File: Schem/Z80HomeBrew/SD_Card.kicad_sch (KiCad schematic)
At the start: 4 parts, among them J2 Micro_SD_Card_Det1, U17 4050

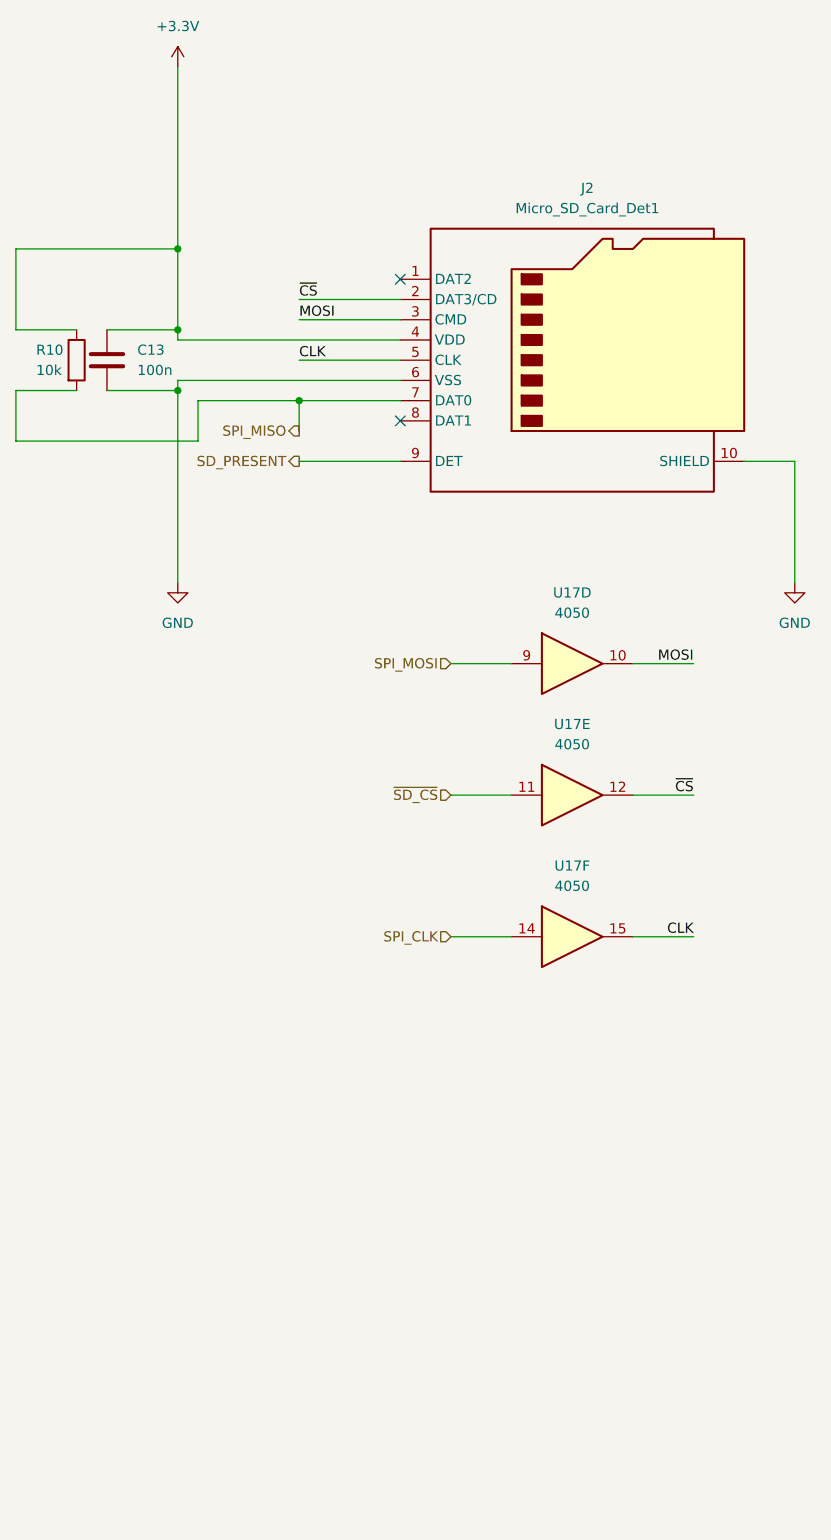
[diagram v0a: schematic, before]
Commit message: Video block added. fixed some issues with parts...
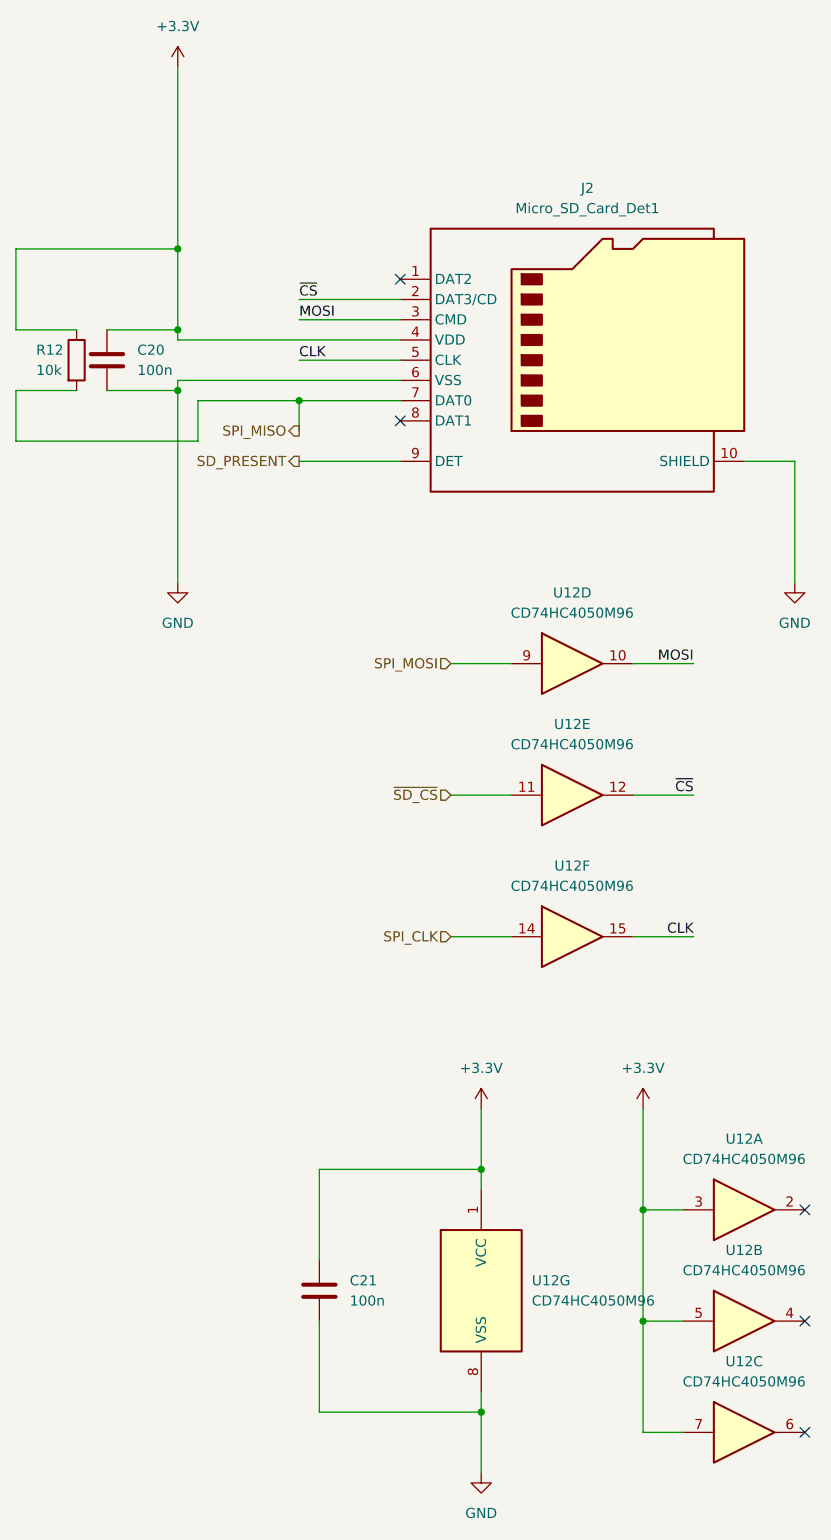
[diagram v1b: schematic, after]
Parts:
- added C21: 100n, Capacitor_SMD:C_0603_1608Metric, symbol Device:C
- added unit 3 of U12
- added unit 1 of U12
- added unit 7 of U12
- added unit 2 of U12
- U12: renamed from U17; value 4050 -> CD74HC4050M96; footprint (none) -> Footprints:SOIC127P600X175-16N
- renumbered C13 to C20, R10 to R12
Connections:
- net +3.3V: now also C21.1, U12.1 (VCC), U12.3, U12.5, U12.7
- net GND: now also C21.2, U12.8 (VSS)
- no-connect marks 2 -> 5

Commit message: Completed schematics
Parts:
- J2: value Micro_SD_Card_Det1 -> MSD-1-A; footprint (none) -> Footprints:CUI_MSD-1-A
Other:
- moved on the sheet: C21, R12, U12G
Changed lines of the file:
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@@
 	)
 	(junction
-		(at 88.9 195.58)
+		(at 83.82 195.58)
 		(diameter 0)
 		(color 0 0 0 0)
@@
 	)
 	(junction
-		(at 88.9 165.1)
+		(at 83.82 165.1)
 		(diameter 0)
 		(color 0 0 0 0)
@@
 	(wire
 		(pts
-			(xy 30.48 67.31) (xy 38.1 67.31)
-		)
-		(stroke
-			(width 0)
-			(type default)
-		)
-	)
-	(wire
-		(pts
 			(xy 128.27 76.2) (xy 128.27 91.44)
 		)
@@
 	(wire
 		(pts
-			(xy 88.9 165.1) (xy 88.9 167.64)
+			(xy 83.82 165.1) (xy 83.82 167.64)
 		)
 		(stroke
@@
 	(wire
 		(pts
-			(xy 88.9 157.48) (xy 88.9 165.1)
+			(xy 83.82 157.48) (xy 83.82 165.1)
 		)
 		(stroke
@@
 	(wire
 		(pts
-			(xy 30.48 67.31) (xy 30.48 73.66)
-		)
-		(stroke
-			(width 0)
-			(type default)
-		)
-	)
-	(wire
-		(pts
-			(xy 88.9 193.04) (xy 88.9 195.58)
+			(xy 36.83 67.31) (xy 36.83 73.66)
+		)
+		(stroke
+			(width 0)
+			(type default)
+		)
+	)
+	(wire
+		(pts
+			(xy 83.82 193.04) (xy 83.82 195.58)
 		)
 		(stroke
@@
 	(wire
 		(pts
-			(xy 68.58 165.1) (xy 88.9 165.1)
+			(xy 63.5 165.1) (xy 83.82 165.1)
 		)
 		(stroke
@@
 	(wire
 		(pts
-			(xy 30.48 49.53) (xy 50.8 49.53)
+			(xy 36.83 49.53) (xy 50.8 49.53)
 		)
 		(stroke
@@
 	(wire
 		(pts
-			(xy 30.48 59.69) (xy 38.1 59.69)
-		)
-		(stroke
-			(width 0)
-			(type default)
-		)
-	)
-	(wire
-		(pts
 			(xy 66.04 76.2) (xy 78.74 76.2)
 		)
@@
 	(wire
 		(pts
-			(xy 68.58 195.58) (xy 88.9 195.58)
+			(xy 63.5 195.58) (xy 83.82 195.58)
 		)
 		(stroke
@@
 	(wire
 		(pts
-			(xy 30.48 73.66) (xy 53.34 73.66)
-		)
-		(stroke
-			(width 0)
-			(type default)
-		)
-	)
-	(wire
-		(pts
-			(xy 68.58 184.15) (xy 68.58 195.58)
+			(xy 36.83 73.66) (xy 53.34 73.66)
+		)
+		(stroke
+			(width 0)
+			(type default)
+		)
+	)
+	(wire
+		(pts
+			(xy 63.5 184.15) (xy 63.5 195.58)
 		)
 		(stroke
@@
 	(wire
 		(pts
-			(xy 30.48 59.69) (xy 30.48 49.53)
-		)
-		(stroke
-			(width 0)
-			(type default)
-		)
-	)
-	(wire
-		(pts
-			(xy 68.58 176.53) (xy 68.58 165.1)
+			(xy 36.83 59.69) (xy 36.83 49.53)
+		)
+		(stroke
+			(width 0)
+			(type default)
+		)
+	)
+	(wire
+		(pts
+			(xy 63.5 176.53) (xy 63.5 165.1)
 		)
 		(stroke
@@
 	(wire
 		(pts
-			(xy 88.9 195.58) (xy 88.9 203.2)
+			(xy 83.82 195.58) (xy 83.82 203.2)
 		)
 		(stroke
@@
 			)
 		)
-		(property "Value" "Micro_SD_Card_Det1"
+		(property "Value" "MSD-1-A"
 			(at 102.235 44.45 0)
 			(effects
@@
 			)
 		)
-		(property "Footprint" ""
+		(property "Footprint" "Footprints:CUI_MSD-1-A"
 			(at 153.67 45.72 0)
 			(effects
@@
 			)
 		)
-		(property "Datasheet" "https://datasheet.lcsc.com/lcsc/2110151630_XKB-Connectivity-XKTF-015-N_C381082.pdf"
+		(property "Datasheet" "https://www.sameskydevices.com/product/resource/msd-4-a.pdf"
 			(at 101.6 60.96 0)
 			(effects
@@
 	(symbol
 		(lib_id "Device:C")
-		(at 68.58 180.34 0)
+		(at 63.5 180.34 0)
 		(unit 1)
 		(exclude_from_sim no)
@@
 		(fields_autoplaced yes)
 		(property "Reference" "C21"
-			(at 72.39 179.0699 0)
+			(at 67.31 179.0699 0)
 			(effects
 				(font
@@
 		)
 		(property "Value" "100n"
-			(at 72.39 181.6099 0)
+			(at 67.31 181.6099 0)
 			(effects
 				(font
@@
 		)
 		(property "Footprint" "Capacitor_SMD:C_0603_1608Metric"
-			(at 69.5452 184.15 0)
+			(at 64.4652 184.15 0)
 			(effects
 				(font
@@
 		)
 		(property "Datasheet" "~"
-			(at 68.58 180.34 0)
+			(at 63.5 180.34 0)
 			(effects
 				(font
@@
 		)
 		(property "Description" "Unpolarized capacitor"
-			(at 68.58 180.34 0)
+			(at 63.5 180.34 0)
 			(effects
 				(font
@@
 	(symbol
 		(lib_id "power:+3.3V")
-		(at 88.9 157.48 0)
+		(at 83.82 157.48 0)
 		(unit 1)
 		(exclude_from_sim no)
@@
 		(fields_autoplaced yes)
 		(property "Reference" "#PWR051"
-			(at 88.9 161.29 0)
+			(at 83.82 161.29 0)
 			(effects
 				(font
@@
 		)
 		(property "Value" "+3.3V"
-			(at 88.9 152.4 0)
+			(at 83.82 152.4 0)
 			(effects
 				(font
@@
 		)
 		(property "Footprint" ""
-			(at 88.9 157.48 0)
+			(at 83.82 157.48 0)
 			(effects
 				(font
@@
 		)
 		(property "Datasheet" ""
-			(at 88.9 157.48 0)
+			(at 83.82 157.48 0)
 			(effects
 				(font
@@
 		)
 		(property "Description" "Power symbol creates a global label with name \"+3.3V\""
-			(at 88.9 157.48 0)
+			(at 83.82 157.48 0)
 			(effects
 				(font
@@
 	(symbol
 		(lib_id "Device:R")
-		(at 38.1 63.5 0)
+		(at 36.83 63.5 0)
 		(unit 1)
 		(exclude_from_sim no)
@@
 		(dnp no)
 		(property "Reference" "R12"
-			(at 33.02 62.2299 0)
+			(at 31.75 62.2299 0)
 			(effects
 				(font
@@
 		)
 		(property "Value" "10k"
-			(at 33.02 64.7699 0)
+			(at 31.75 64.7699 0)
 			(effects
 				(font
@@
 		)
 		(property "Footprint" "Resistor_SMD:R_0603_1608Metric"
-			(at 36.322 63.5 90)
+			(at 35.052 63.5 90)
 			(effects
 				(font
@@
 		)
 		(property "Datasheet" "~"
-			(at 38.1 63.5 0)
+			(at 36.83 63.5 0)
 			(effects
 				(font
@@
 		)
 		(property "Description" "Resistor"
-			(at 38.1 63.5 0)
+			(at 36.83 63.5 0)
 			(effects
 				(font
@@
 	(symbol
 		(lib_id "4xxx:4050")
-		(at 88.9 180.34 0)
+		(at 83.82 180.34 0)
 		(unit 7)
 		(exclude_from_sim no)
@@
 		(fields_autoplaced yes)
 		(property "Reference" "U12"
-			(at 95.25 179.0699 0)
+			(at 90.17 179.0699 0)
 			(effects
 				(font
@@
 		)
 		(property "Value" "CD74HC4050M96"
-			(at 95.25 181.6099 0)
+			(at 90.17 181.6099 0)
 			(effects
 				(font
@@
 		)
 		(property "Footprint" "Footprints:SOIC127P600X175-16N"
-			(at 88.9 180.34 0)
+			(at 83.82 180.34 0)
 			(effects
 				(font
@@
 		)
 		(property "Datasheet" "http://www.intersil.com/content/dam/intersil/documents/cd40/cd4050bms.pdf"
-			(at 88.9 180.34 0)
+			(at 83.82 180.34 0)
 			(effects
 				(font
@@
 		)
 		(property "Description" "Hex Buffer"
-			(at 88.9 180.34 0)
+			(at 83.82 180.34 0)
 			(effects
 				(font
@@
 	(symbol
 		(lib_id "power:GND")
-		(at 88.9 203.2 0)
+		(at 83.82 203.2 0)
 		(unit 1)
 		(exclude_from_sim no)
@@
 		(fields_autoplaced yes)
 		(property "Reference" "#PWR053"
-			(at 88.9 209.55 0)
+			(at 83.82 209.55 0)
 			(effects
 				(font
@@
 		)
 		(property "Value" "GND"
-			(at 88.9 208.28 0)
+			(at 83.82 208.28 0)
 			(effects
 				(font
@@
 		)
 		(property "Footprint" ""
-			(at 88.9 203.2 0)
+			(at 83.82 203.2 0)
 			(effects
 				(font
@@
 		)
 		(property "Datasheet" ""
-			(at 88.9 203.2 0)
+			(at 83.82 203.2 0)
 			(effects
 				(font
@@
 		)
 		(property "Description" "Power symbol creates a global label with name \"GND\" , ground"
-			(at 88.9 203.2 0)
-			(effects
-				(font
+			(at 83.82 203.2 0)
+			(effects
+				(font

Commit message: Finally found a name "Zephyr-80" for the brew and committing the first pbc
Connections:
- net +3.3V: no longer U12.3, U12.5, U12.7
- net GND: now also U12.3, U12.5, U12.7
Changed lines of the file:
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@@
+	)
+	(junction
+		(at 109.22 198.12)
+		(diameter 0)
+		(color 0 0 0 0)
 	)
 	(junction
@@
 		(color 0 0 0 0)
 	)
-	(junction
-		(at 109.22 170.18)
-		(diameter 0)
-		(color 0 0 0 0)
-	)
 	(no_connect
 		(at 129.54 170.18)
@@
 	(wire
 		(pts
+			(xy 109.22 198.12) (xy 109.22 203.2)
+		)
+		(stroke
+			(width 0)
+			(type default)
+		)
+	)
+	(wire
+		(pts
 			(xy 78.74 66.04) (xy 50.8 66.04)
 		)
@@
 		(pts
 			(xy 53.34 73.66) (xy 53.34 68.58)
-		)
-		(stroke
-			(width 0)
-			(type default)
-		)
-	)
-	(wire
-		(pts
-			(xy 109.22 157.48) (xy 109.22 170.18)
 		)
 		(stroke
@@
 	)
 	(symbol
-		(lib_id "power:+3.3V")
-		(at 109.22 157.48 0)
+		(lib_id "power:GND")
+		(at 109.22 203.2 0)
 		(unit 1)
 		(exclude_from_sim no)
@@
 		(fields_autoplaced yes)
 		(property "Reference" "#PWR052"
-			(at 109.22 161.29 0)
-			(effects
-				(font
-					(size 1.27 1.27)
-				)
-				(hide yes)
-			)
-		)
-		(property "Value" "+3.3V"
-			(at 109.22 152.4 0)
+			(at 109.22 209.55 0)
+			(effects
+				(font
+					(size 1.27 1.27)
+				)
+				(hide yes)
+			)
+		)
+		(property "Value" "GND"
+			(at 109.22 208.28 0)
 			(effects
 				(font
@@
 		)
 		(property "Footprint" ""
-			(at 109.22 157.48 0)
+			(at 109.22 203.2 0)
 			(effects
 				(font
@@
 		)
 		(property "Datasheet" ""
-			(at 109.22 157.48 0)
-			(effects
-				(font
-					(size 1.27 1.27)
-				)
-				(hide yes)
-			)
-		)
-		(property "Description" "Power symbol creates a global label with name \"+3.3V\""
-			(at 109.22 157.48 0)
-			(effects
-				(font
+			(at 109.22 203.2 0)
+			(effects
+				(font
+					(size 1.27 1.27)
+				)
+				(hide yes)
+			)
+		)
+		(property "Description" "Power symbol creates a global label with name \"GND\" , ground"
+			(at 109.22 203.2 0)
+			(effects
+				(font

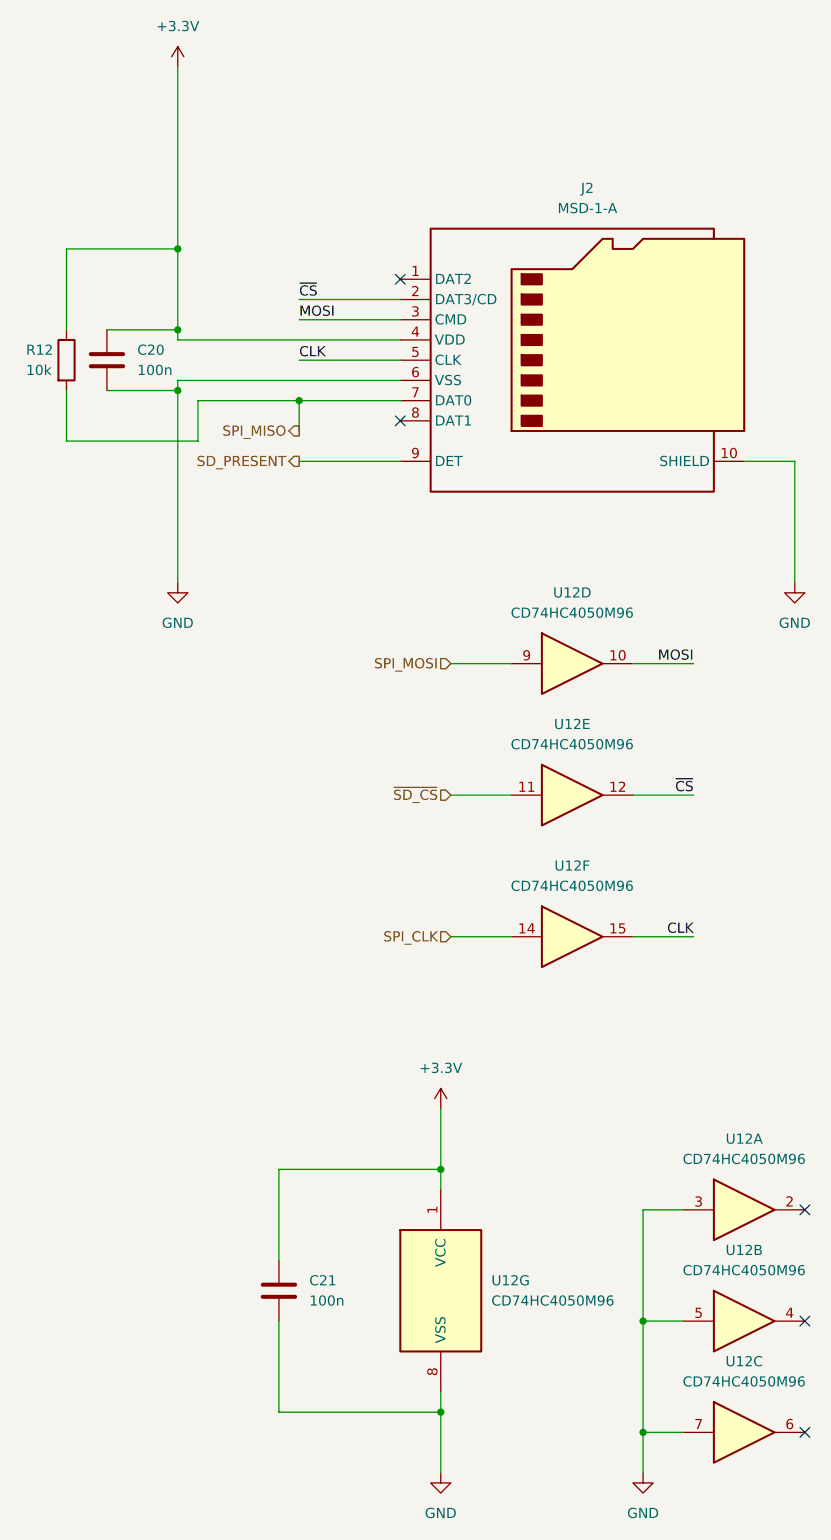
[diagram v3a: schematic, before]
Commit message: Added pBITzBackplane and MezzanineConnector
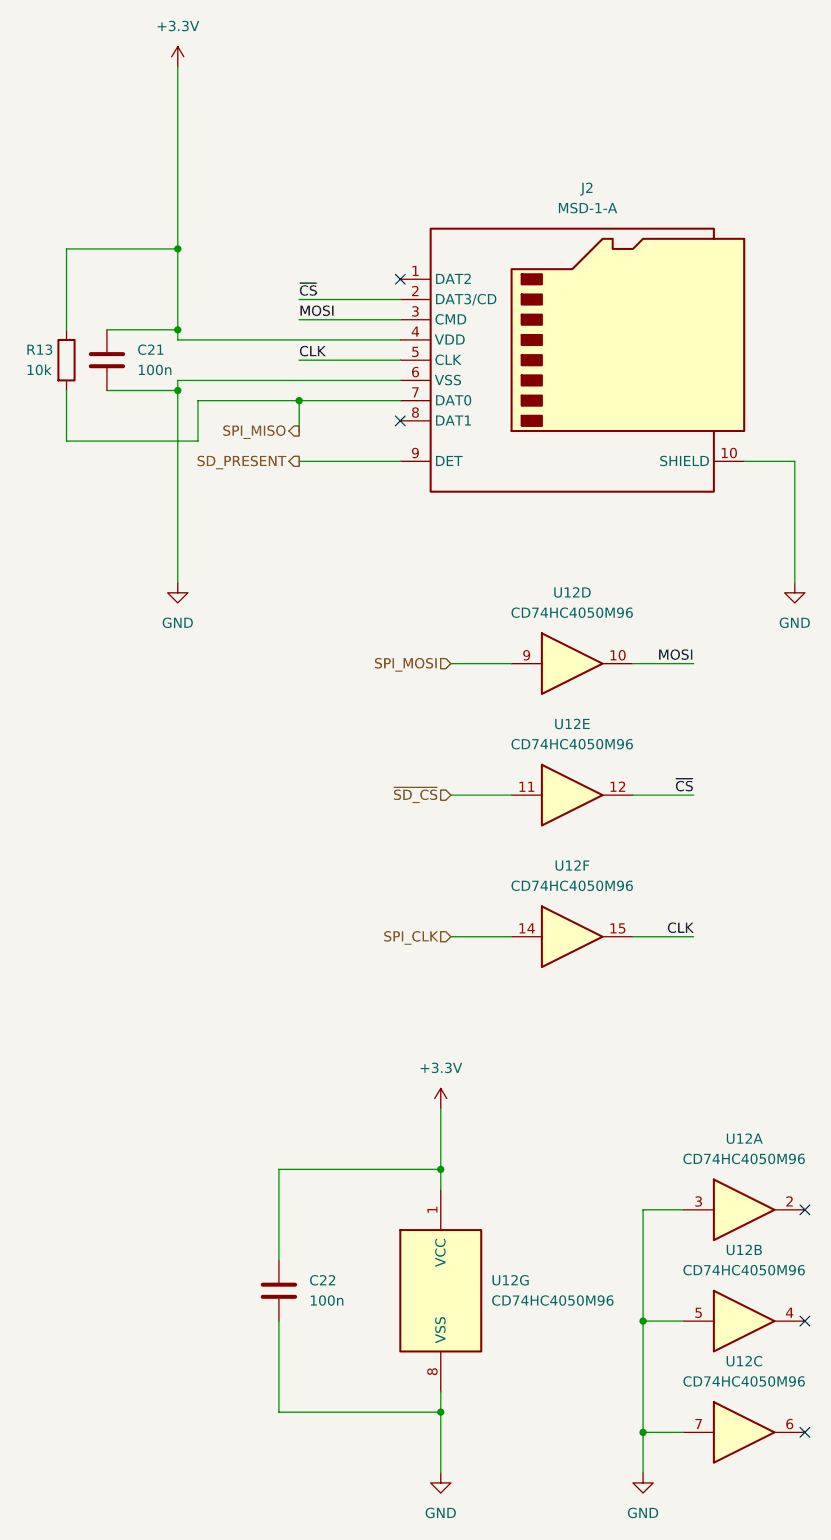
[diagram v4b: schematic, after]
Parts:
- C21: renamed from C20; MANUFACTURER_PART_NUMBER (none) -> C0603C104K5RACTU
- C22: renamed from C21; MANUFACTURER_PART_NUMBER (none) -> C0603C104K5RACTU
- J2: MANUFACTURER_PART_NUMBER (none) -> MSD-1-A
- R13: renamed from R12; MANUFACTURER_PART_NUMBER (none) -> RC0603FR-0710KL
- U12: MANUFACTURER_PART_NUMBER (none) -> CD74HC4050M96
